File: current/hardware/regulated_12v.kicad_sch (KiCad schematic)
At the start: 20 parts, among them U7 LM339LV, U8 TPS61085DGKR, U9 TPS2553DBVR-1

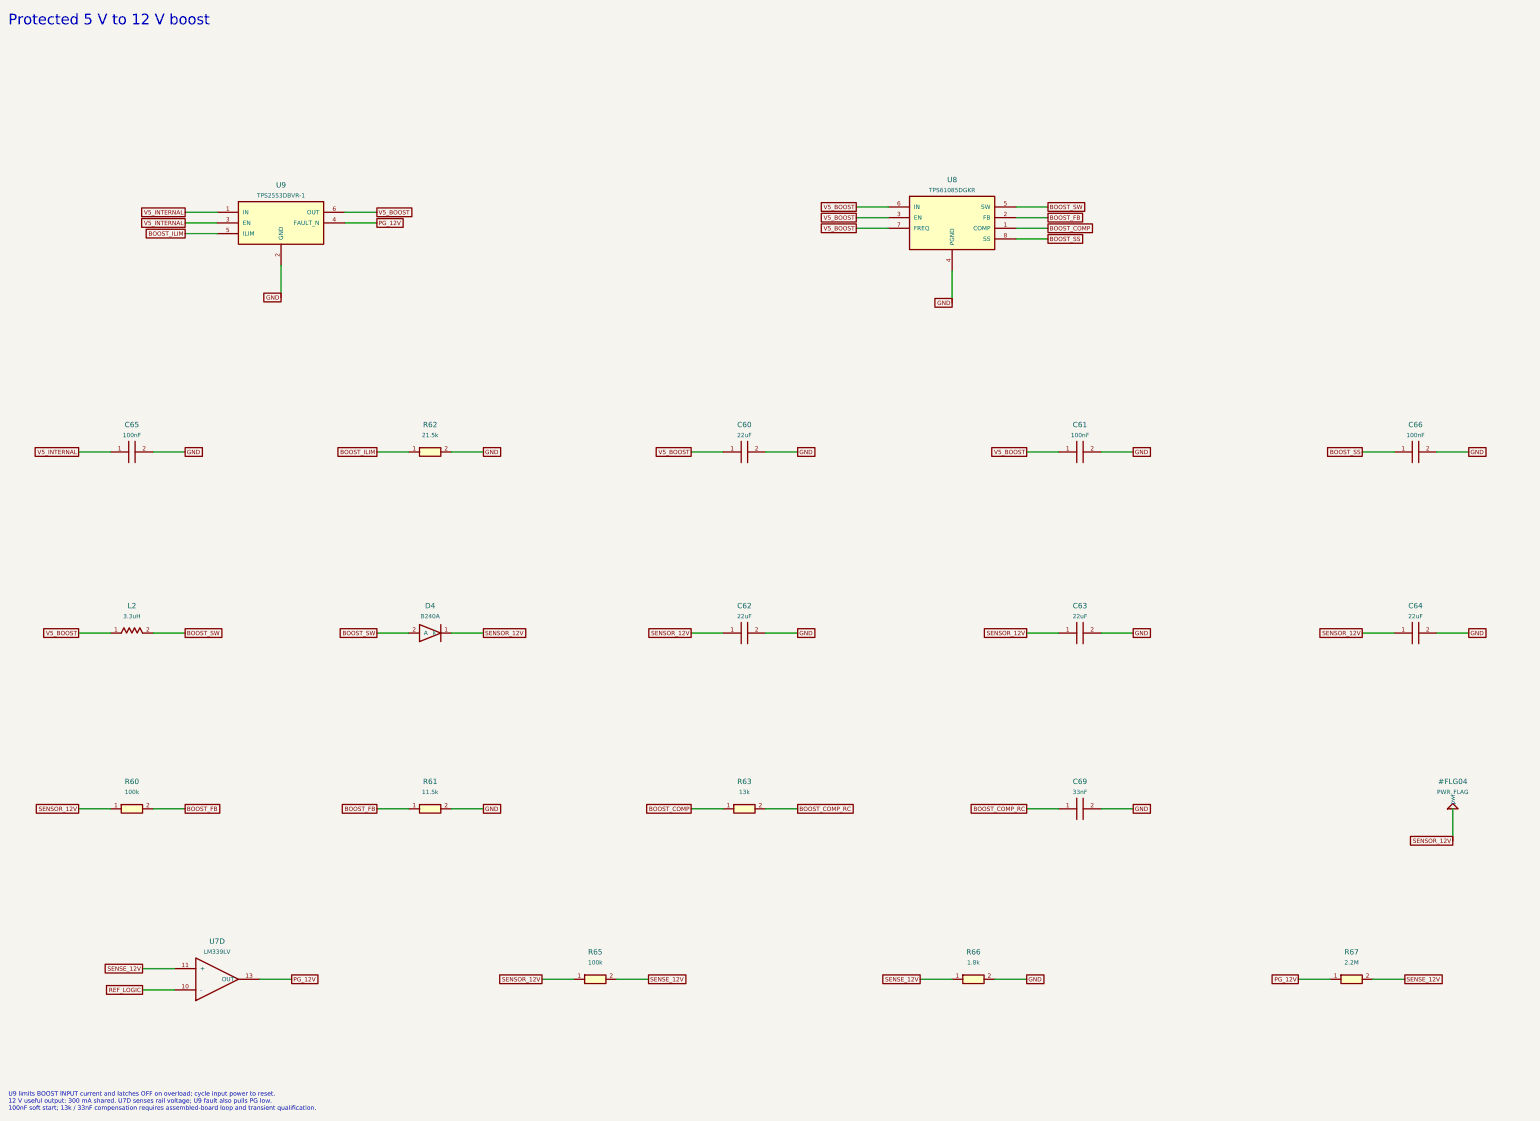
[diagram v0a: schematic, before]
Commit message: Rev G: protect sensor power and verify startup and fault recovery
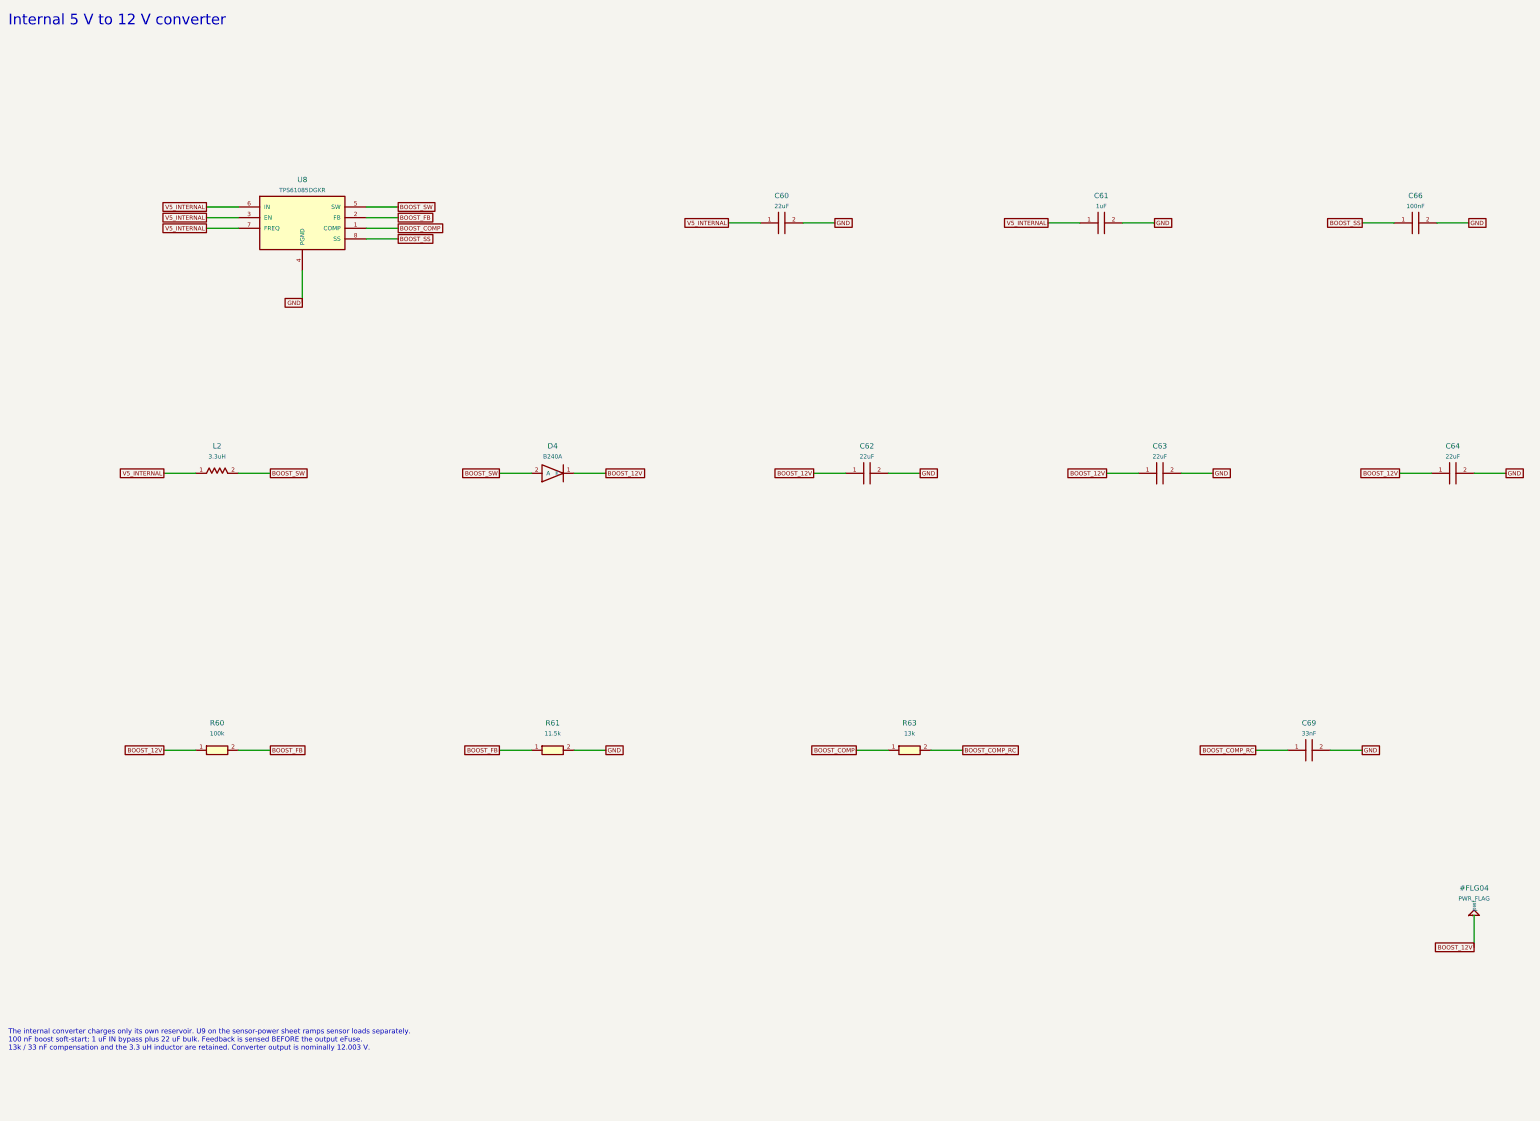
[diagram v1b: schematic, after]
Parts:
- removed C65: 100nF, FRC_Sensor_CAN:C_0805_2012Metric, symbol FRC_Sensor_CAN:C
- removed R62: 21.5k, FRC_Sensor_CAN:R_0805_2012Metric, symbol FRC_Sensor_CAN:R
- removed R65: 100k, FRC_Sensor_CAN:R_0805_2012Metric, symbol FRC_Sensor_CAN:R
- removed R66: 1.8k, FRC_Sensor_CAN:R_0805_2012Metric, symbol FRC_Sensor_CAN:R
- removed R67: 2.2M, FRC_Sensor_CAN:R_0805_2012Metric, symbol FRC_Sensor_CAN:R
- removed U7: LM339LV, FRC_Sensor_CAN:SOIC-14_3.9x8.7mm_P1.27mm, symbol FRC_Sensor_CAN:COMP4
- removed U9: TPS2553DBVR-1, FRC_Sensor_CAN:SOT-23-6, symbol FRC_Sensor_CAN:LOADSW
- C61: value 100nF -> 1uF; MPN CL21B104KCFNNNE -> CL21B105KBFNNNE; Notes Local decoupling. -> 1uF local TPS61085 IN bypass, adjacent to U8; C60 provides 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
- C66: Notes 100nF soft-start; qualify startup with full sensor capacita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 -> Boost soft-start charges only the local reservoir; external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
- D4: Notes 2A 40V Schottky rectifier; cathode on SENSOR_12V. U9 interr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 -> 2A 40V Schottky rectifier; cathode on BOOST_12V, before U9 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
- L2: Notes 3.3uH; retained 5A RMS / 8A saturation part, above 3.2A max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 -> 3.3uH; 5A RMS and 8A at 20% inductance loss. Output eFuse p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
- U8: Notes 5 V to 12 V nonsynchronous boost; 1.2 MHz. Branch input dis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 -> 5 V-fed boost, 1.2 MHz. Its output reservoir is isolated fr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
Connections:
- net V5_BOOST is gone; now on net V5_INTERNAL: C60.1, C61.1, L2.1, U8.3 (EN), U8.6 (IN), U8.7 (FREQ)
- net SENSOR_12V renamed BOOST_12V
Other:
- note added: "Internal 5 V to 12 V converter"
- note added: "The internal converter charges only its own reservoir. U9 on the sensor-power sheet ramps sensor loads separately. 100 nF boost soft-start; 1 uF IN bypass plus 22 uF bulk. Feedback is sensed BEFORE the output eFuse. 13k / 33 nF compensation and the 3.3 uH inductor are retained. Converter output is nominally 12.003 V."
- note removed: "Protected 5 V to 12 V boost"
- note removed: "U9 limits BOOST INPUT current and latches OFF on overload; cycle input power to reset. 12 V useful output: 300 mA shared. U7D senses rail voltage; U9 fault also pulls PG low. 100nF soft start; 13k / 33nF compensation requires assembled-board loop and transient qualification."
- title: SC12 - Protected 5 V to 12 V boost -> SC12 - Internal 5 V to 12 V converter
- moved on the sheet: C60, C61, C62, C63, C64, C66, C69, D4, L2, R60, R61, R63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

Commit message: Prepare JLC-matched Rev H sourcing candidate pending simulation approval
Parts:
- R61: MPN RC0805FR-0711K5L -> 0805W8F1152T5E
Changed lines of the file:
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@@
 (wire (pts (xy 149.86 190.5) (xy 157.48 190.5)) (stroke (width 0) (type default)))
 (global_label "GND" (shape passive) (at 157.48 190.5 180) (effects (font (size 1.016 1.016)) (justify left)) (property "Intersheetrefs" "${INTERSHEET_REFS}" (at 157.48 190.5 0) (effects (font (size 1.27 1.27)) (hide yes))))
-(symbol (lib_id "FRC_Sensor_CAN:R") (at 144.78 190.5 0) (unit 1) (in_bom yes) (on_board yes) (dnp no) (property "Reference" "R61" (at 144.78 184 0) (effects (font (size 1.27 1.27))))(property "Value" "11.5k" (at 144.78 186.5 0) (effects (font (size 1.016 1.016))))(property "Footprint" "FRC_Sensor_CAN:R_0805_2012Metric" (at 144.78 190.5 0) (effects (font (size 1.27 1.27)) (hide yes)))(property "Datasheet" "" (at 144.78 190.5 0) (effects (font (size 1.27 1.27)) (hide yes)))(property "MPN" "RC0805FR-0711K5L" (at 144.78 190.5 0) (effects (font (size 1.27 1.27)) (hide yes)))(property "Notes" "Feedback lower arm, 1%. 12.003V nominal with 1.238V reference." (at 144.78 190.5 0) (effects (font (size 1.27 1.27)) (hide yes)))(pin "1")(pin "2")(instances (project "FRC_Sensor_CAN" (path "/32fd904d-6274-5c4e-88d3-bb1b48cbb6d1/a8b6029a-2c88-53a0-ae51-a49b2408ffb7" (reference "R61") (unit 1)))) )
+(symbol (lib_id "FRC_Sensor_CAN:R") (at 144.78 190.5 0) (unit 1) (in_bom yes) (on_board yes) (dnp no) (property "Reference" "R61" (at 144.78 184 0) (effects (font (size 1.27 1.27))))(property "Value" "11.5k" (at 144.78 186.5 0) (effects (font (size 1.016 1.016))))(property "Footprint" "FRC_Sensor_CAN:R_0805_2012Metric" (at 144.78 190.5 0) (effects (font (size 1.27 1.27)) (hide yes)))(property "Datasheet" "" (at 144.78 190.5 0) (effects (font (size 1.27 1.27)) (hide yes)))(property "MPN" "0805W8F1152T5E" (at 144.78 190.5 0) (effects (font (size 1.27 1.27)) (hide yes)))(property "Notes" "Feedback lower arm, 1%. 12.003V nominal with 1.238V reference." (at 144.78 190.5 0) (effects (font (size 1.27 1.27)) (hide yes)))(pin "1")(pin "2")(instances (project "FRC_Sensor_CAN" (path "/32fd904d-6274-5c4e-88d3-bb1b48cbb6d1/a8b6029a-2c88-53a0-ae51-a49b2408ffb7" (reference "R61") (unit 1)))) )
 (wire (pts (xy 224.79 190.5) (xy 217.17 190.5)) (stroke (width 0) (type default)))
 (global_label "BOOST_COMP" (shape passive) (at 217.17 190.5 0) (effects (font (size 1.016 1.016)) (justify right)) (property "Intersheetrefs" "${INTERSHEET_REFS}" (at 217.17 190.5 0) (effects (font (size 1.27 1.27)) (hide yes))))
